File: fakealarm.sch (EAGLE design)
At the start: 14 parts, among them IC1 NE555N, Q1 2N3904, X1 RUN, X2 BAT, X3 GND

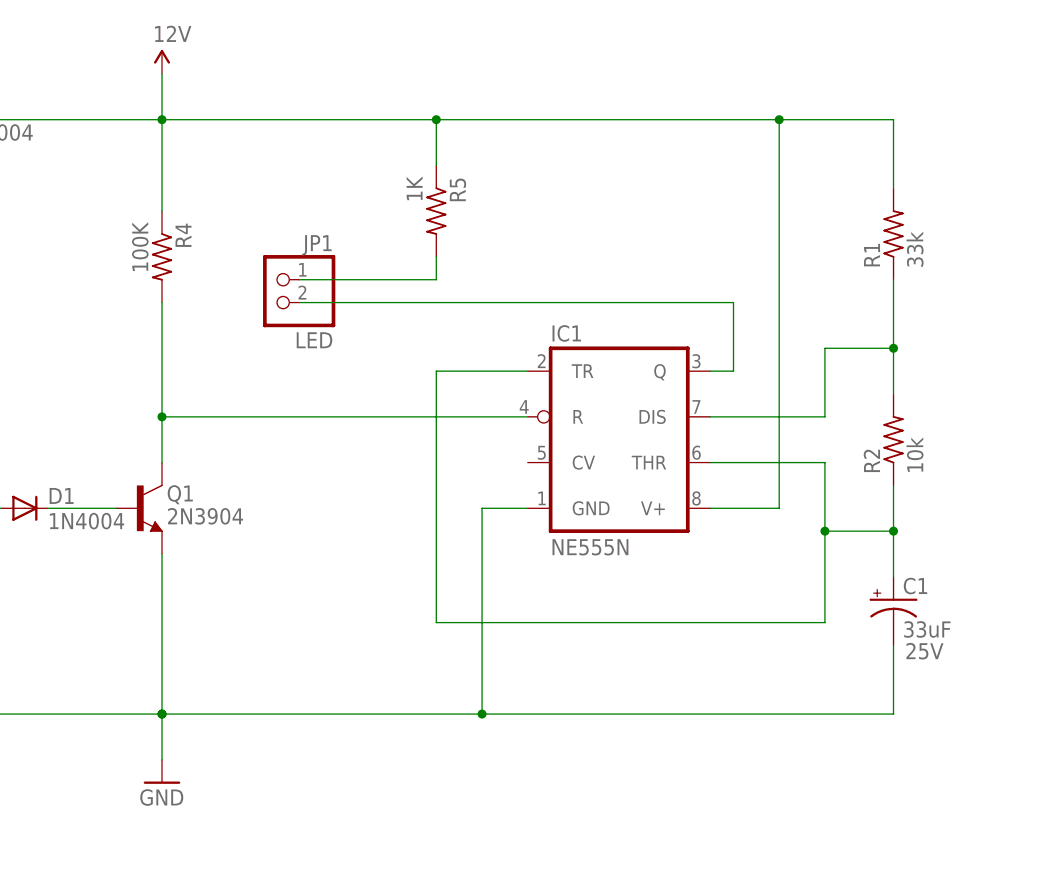
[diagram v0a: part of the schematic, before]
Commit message: Added 10nF (0.01uF) bypass on CV, shrank board, moved components around a little
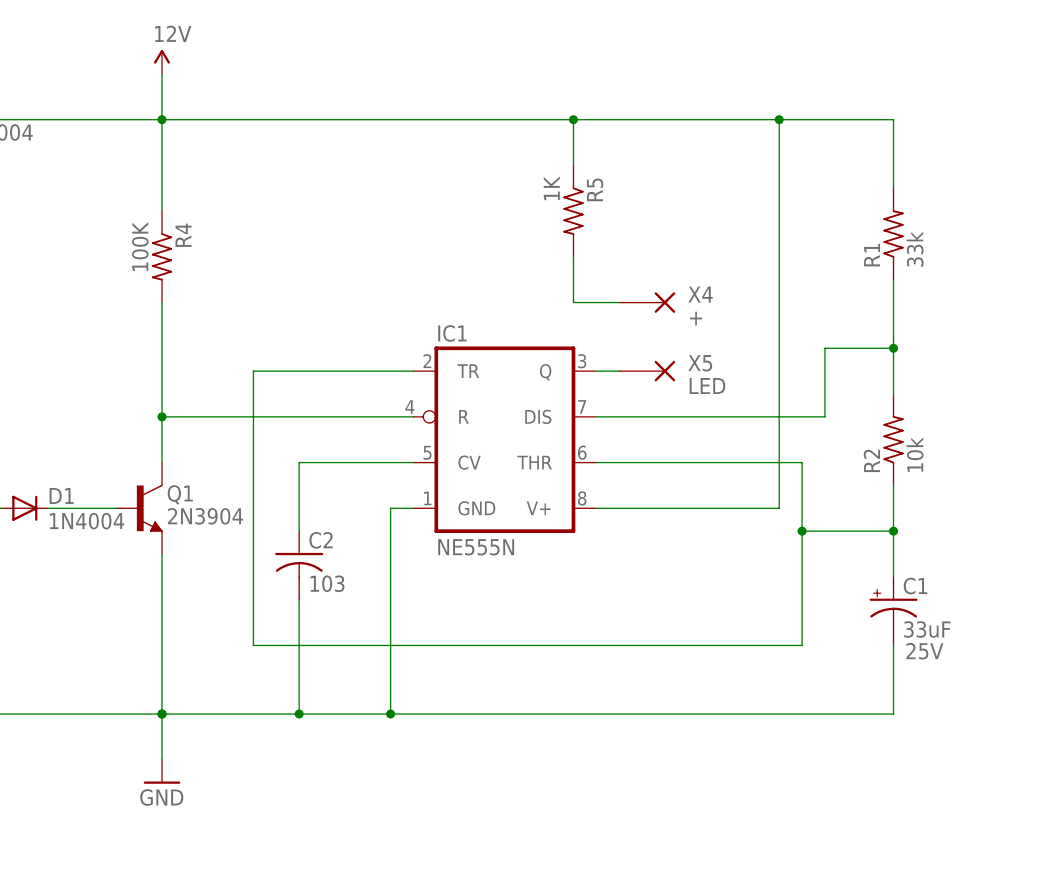
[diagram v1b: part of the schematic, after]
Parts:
- removed JP1: LED, pinhead-2:PINHD-1X02_2.54-S
- added C2: 103, rcl:C-US050-024X044
- added X4: +, bt_electromech:WIREPAD_24GA
- added X5: LED, bt_electromech:WIREPAD_24GA
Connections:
- new net N$7: C2.1, IC1.CV
- net GND: now also C2.2
- net N$10: now also X5.P; no longer JP1.2
- net N$9: now also X4.P; no longer JP1.1
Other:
- moved on the sheet: IC1, R5
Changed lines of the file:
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@@
 <attribute name="VOLTAGE" value="25V"/>
 </part>
-<part name="JP1" library="pinhead-2" deviceset="PINHD-1X02" device="_2.54-S" value="LED"/>
 <part name="SUPPLY1" library="SparkFun-Aesthetics" deviceset="12V" device=""/>
 <part name="GND4" library="bt" deviceset="GND" device=""/>
@@
 <part name="D2" library="diode" deviceset="1N4004" device=""/>
 <part name="FRAME1" library="bt" deviceset="LETTER_L" device=""/>
+<part name="X4" library="bt_electromech" deviceset="WIREPAD" device="_24GA" value="+"/>
+<part name="X5" library="bt_electromech" deviceset="WIREPAD" device="_24GA" value="LED"/>
+<part name="C2" library="rcl" deviceset="C-US" device="050-024X044" value="103"/>
 </parts>
 <sheets>
@@
 </plain>
 <instances>
-<instance part="IC1" gate="A" x="160.02" y="104.14"/>
+<instance part="IC1" gate="A" x="147.32" y="104.14"/>
 <instance part="Q1" gate="G1" x="106.68" y="96.52"/>
 <instance part="R1" gate="G$1" x="190.5" y="127" rot="R90"/>
@@
 <instance part="R3" gate="G$1" x="83.82" y="96.52" rot="R180"/>
 <instance part="R4" gate="G$1" x="109.22" y="124.46" rot="R270"/>
-<instance part="R5" gate="G$1" x="139.7" y="129.54" rot="R270"/>
+<instance part="R5" gate="G$1" x="154.94" y="129.54" rot="R270"/>
 <instance part="C1" gate="G$1" x="190.5" y="86.36">
 <attribute name="VOLTAGE" x="191.77" y="79.756" size="1.778" layer="96"/>
 </instance>
-<instance part="JP1" gate="A" x="121.92" y="119.38" rot="MR0"/>
 <instance part="SUPPLY1" gate="G$1" x="109.22" y="144.78"/>
 <instance part="GND4" gate="1" x="109.22" y="66.04"/>
@@
 <instance part="FRAME1" gate="G$1" x="0" y="0"/>
 <instance part="FRAME1" gate="G$2" x="147.32" y="2.54"/>
+<instance part="X4" gate="G$1" x="165.1" y="119.38"/>
+<instance part="X5" gate="G$1" x="165.1" y="111.76"/>
+<instance part="C2" gate="G$1" x="124.46" y="91.44"/>
 </instances>
 <busses>
@@
 <pinref part="IC1" gate="A" pin="DIS"/>
 <wire x1="190.5" y1="114.3" x2="190.5" y2="109.22" width="0.1524" layer="91"/>
-<wire x1="170.18" y1="106.68" x2="182.88" y2="106.68" width="0.1524" layer="91"/>
+<wire x1="157.48" y1="106.68" x2="182.88" y2="106.68" width="0.1524" layer="91"/>
 <wire x1="182.88" y1="106.68" x2="182.88" y2="114.3" width="0.1524" layer="91"/>
 <wire x1="182.88" y1="114.3" x2="190.5" y2="114.3" width="0.1524" layer="91"/>
@@
 <pinref part="IC1" gate="A" pin="TR"/>
 <wire x1="190.5" y1="93.98" x2="190.5" y2="99.06" width="0.1524" layer="91"/>
-<wire x1="149.86" y1="111.76" x2="139.7" y2="111.76" width="0.1524" layer="91"/>
-<wire x1="139.7" y1="111.76" x2="139.7" y2="83.82" width="0.1524" layer="91"/>
-<wire x1="139.7" y1="83.82" x2="182.88" y2="83.82" width="0.1524" layer="91"/>
-<wire x1="182.88" y1="83.82" x2="182.88" y2="93.98" width="0.1524" layer="91"/>
-<wire x1="182.88" y1="93.98" x2="190.5" y2="93.98" width="0.1524" layer="91"/>
+<wire x1="137.16" y1="111.76" x2="119.38" y2="111.76" width="0.1524" layer="91"/>
+<wire x1="119.38" y1="111.76" x2="119.38" y2="81.28" width="0.1524" layer="91"/>
+<wire x1="119.38" y1="81.28" x2="180.34" y2="81.28" width="0.1524" layer="91"/>
+<wire x1="180.34" y1="81.28" x2="180.34" y2="93.98" width="0.1524" layer="91"/>
+<wire x1="180.34" y1="93.98" x2="190.5" y2="93.98" width="0.1524" layer="91"/>
 <junction x="190.5" y="93.98"/>
 <pinref part="IC1" gate="A" pin="THR"/>
-<wire x1="170.18" y1="101.6" x2="182.88" y2="101.6" width="0.1524" layer="91"/>
-<wire x1="182.88" y1="101.6" x2="182.88" y2="93.98" width="0.1524" layer="91"/>
-<junction x="182.88" y="93.98"/>
+<wire x1="157.48" y1="101.6" x2="180.34" y2="101.6" width="0.1524" layer="91"/>
+<wire x1="180.34" y1="101.6" x2="180.34" y2="93.98" width="0.1524" layer="91"/>
+<junction x="180.34" y="93.98"/>
 </segment>
 </net>
@@
 <junction x="109.22" y="73.66"/>
 <junction x="109.22" y="73.66"/>
-<wire x1="109.22" y1="73.66" x2="144.78" y2="73.66" width="0.1524" layer="91"/>
 <pinref part="C1" gate="G$1" pin="-"/>
-<wire x1="144.78" y1="73.66" x2="190.5" y2="73.66" width="0.1524" layer="91"/>
+<pinref part="C2" gate="G$1" pin="2"/>
+<wire x1="124.46" y1="86.36" x2="124.46" y2="73.66" width="0.1524" layer="91"/>
+<wire x1="124.46" y1="73.66" x2="134.62" y2="73.66" width="0.1524" layer="91"/>
+<wire x1="134.62" y1="73.66" x2="190.5" y2="73.66" width="0.1524" layer="91"/>
 <wire x1="190.5" y1="73.66" x2="190.5" y2="81.28" width="0.1524" layer="91"/>
+<wire x1="109.22" y1="73.66" x2="124.46" y2="73.66" width="0.1524" layer="91"/>
+<junction x="124.46" y="73.66"/>
 <pinref part="IC1" gate="A" pin="GND"/>
-<wire x1="149.86" y1="96.52" x2="144.78" y2="96.52" width="0.1524" layer="91"/>
-<wire x1="144.78" y1="96.52" x2="144.78" y2="73.66" width="0.1524" layer="91"/>
-<junction x="144.78" y="73.66"/>
+<wire x1="137.16" y1="96.52" x2="134.62" y2="96.52" width="0.1524" layer="91"/>
+<wire x1="134.62" y1="96.52" x2="134.62" y2="73.66" width="0.1524" layer="91"/>
+<junction x="134.62" y="73.66"/>
 </segment>
 </net>
 <net name="N$9" class="0">
 <segment>
-<pinref part="JP1" gate="A" pin="1"/>
 <pinref part="R5" gate="G$1" pin="2"/>
-<wire x1="139.7" y1="124.46" x2="139.7" y2="121.92" width="0.1524" layer="91"/>
-<wire x1="139.7" y1="121.92" x2="124.46" y2="121.92" width="0.1524" layer="91"/>
+<wire x1="154.94" y1="124.46" x2="154.94" y2="119.38" width="0.1524" layer="91"/>
+<wire x1="154.94" y1="119.38" x2="160.02" y2="119.38" width="0.1524" layer="91"/>
+<pinref part="X4" gate="G$1" pin="P"/>
 </segment>
 </net>
@@
 <pinref part="R1" gate="G$1" pin="2"/>
 <wire x1="86.36" y1="139.7" x2="109.22" y2="139.7" width="0.1524" layer="91"/>
-<wire x1="109.22" y1="139.7" x2="139.7" y2="139.7" width="0.1524" layer="91"/>
-<wire x1="139.7" y1="139.7" x2="177.8" y2="139.7" width="0.1524" layer="91"/>
+<wire x1="109.22" y1="139.7" x2="154.94" y2="139.7" width="0.1524" layer="91"/>
+<wire x1="154.94" y1="139.7" x2="177.8" y2="139.7" width="0.1524" layer="91"/>
 <wire x1="177.8" y1="139.7" x2="190.5" y2="139.7" width="0.1524" layer="91"/>
 <wire x1="190.5" y1="139.7" x2="190.5" y2="132.08" width="0.1524" layer="91"/>
@@
 <wire x1="109.22" y1="139.7" x2="109.22" y2="144.78" width="0.1524" layer="91"/>
 <pinref part="R5" gate="G$1" pin="1"/>
-<wire x1="139.7" y1="134.62" x2="139.7" y2="139.7" width="0.1524" layer="91"/>
-<junction x="139.7" y="139.7"/>
+<wire x1="154.94" y1="134.62" x2="154.94" y2="139.7" width="0.1524" layer="91"/>
+<junction x="154.94" y="139.7"/>
 <pinref part="IC1" gate="A" pin="V+"/>
-<wire x1="170.18" y1="96.52" x2="177.8" y2="96.52" width="0.1524" layer="91"/>
+<wire x1="157.48" y1="96.52" x2="177.8" y2="96.52" width="0.1524" layer="91"/>
 <wire x1="177.8" y1="96.52" x2="177.8" y2="139.7" width="0.1524" layer="91"/>
 <junction x="177.8" y="139.7"/>
@@
 <segment>
 <pinref part="IC1" gate="A" pin="Q"/>
-<wire x1="170.18" y1="111.76" x2="172.72" y2="111.76" width="0.1524" layer="91"/>
-<wire x1="172.72" y1="111.76" x2="172.72" y2="119.38" width="0.1524" layer="91"/>
-<pinref part="JP1" gate="A" pin="2"/>
-<wire x1="172.72" y1="119.38" x2="124.46" y2="119.38" width="0.1524" layer="91"/>
+<wire x1="157.48" y1="111.76" x2="160.02" y2="111.76" width="0.1524" layer="91"/>
+<pinref part="X5" gate="G$1" pin="P"/>
 </segment>
 </net>
@@
 <segment>
 <pinref part="IC1" gate="A" pin="R"/>
-<wire x1="149.86" y1="106.68" x2="109.22" y2="106.68" width="0.1524" layer="91"/>
+<wire x1="137.16" y1="106.68" x2="109.22" y2="106.68" width="0.1524" layer="91"/>
 <pinref part="Q1" gate="G1" pin="C"/>
 <pinref part="R4" gate="G$1" pin="2"/>
@@
 </segment>
 </net>
+<net name="N$7" class="0">
+<segment>
+<pinref part="IC1" gate="A" pin="CV"/>
+<pinref part="C2" gate="G$1" pin="1"/>
+<wire x1="137.16" y1="101.6" x2="124.46" y2="101.6" width="0.1524" layer="91"/>
+<wire x1="124.46" y1="101.6" x2="124.46" y2="93.98" width="0.1524" layer="91"/>
+</segment>
+</net>

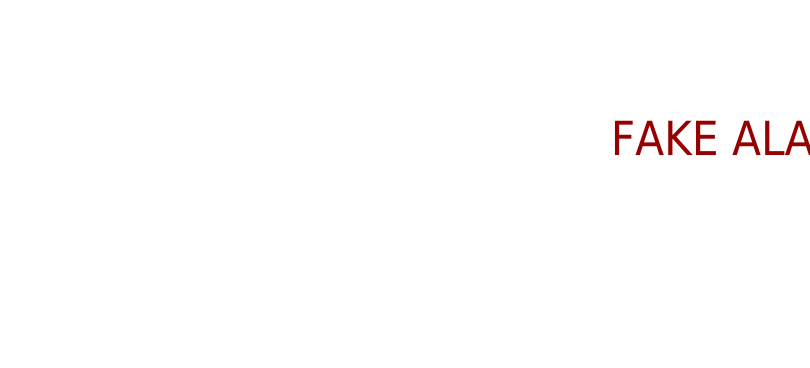
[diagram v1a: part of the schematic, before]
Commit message: added oshw logo, minor silk layout tweaks
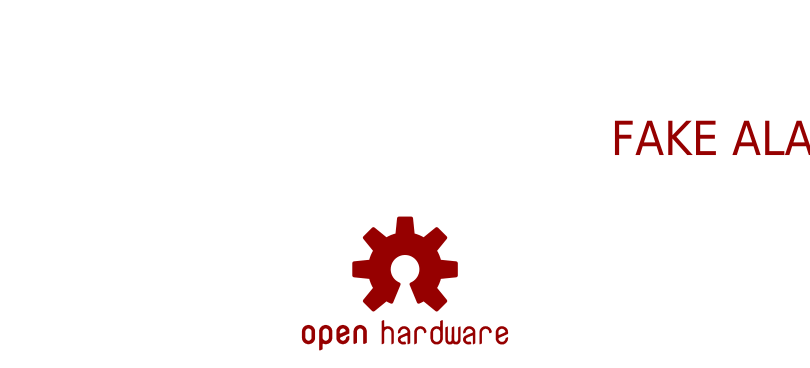
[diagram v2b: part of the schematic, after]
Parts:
- added LOGO1: OSHW-LOGOS, SparkFun-Aesthetics:OSHW-LOGOS
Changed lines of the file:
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@@
 <part name="X5" library="bt_electromech" deviceset="WIREPAD" device="_24GA" value="LED"/>
 <part name="C2" library="rcl" deviceset="C-US" device="050-024X044" value="103"/>
+<part name="LOGO1" library="SparkFun-Aesthetics" deviceset="OSHW-LOGO" device="S" value="OSHW-LOGOS"/>
 </parts>
 <sheets>
@@
 <instance part="X5" gate="G$1" x="165.1" y="111.76"/>
 <instance part="C2" gate="G$1" x="124.46" y="91.44"/>
+<instance part="LOGO1" gate="G$1" x="132.08" y="10.16"/>
 </instances>
 <busses>

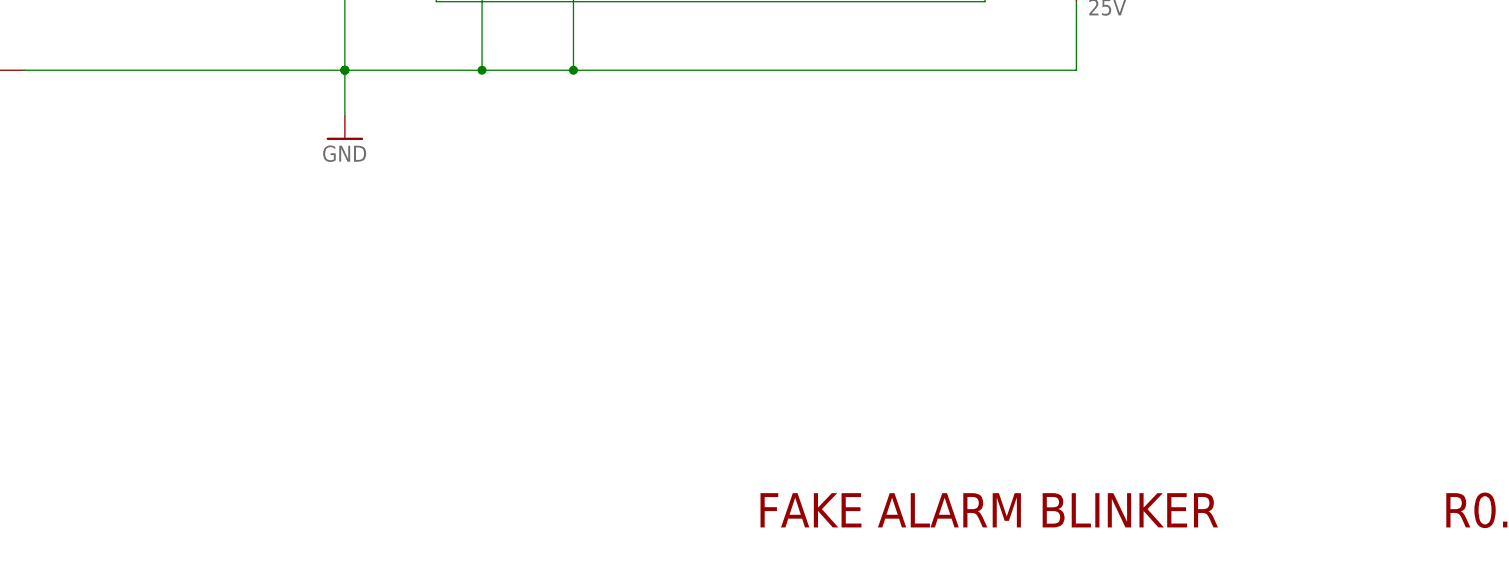
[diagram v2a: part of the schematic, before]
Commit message: Generated silk, added enclosure info to schematic
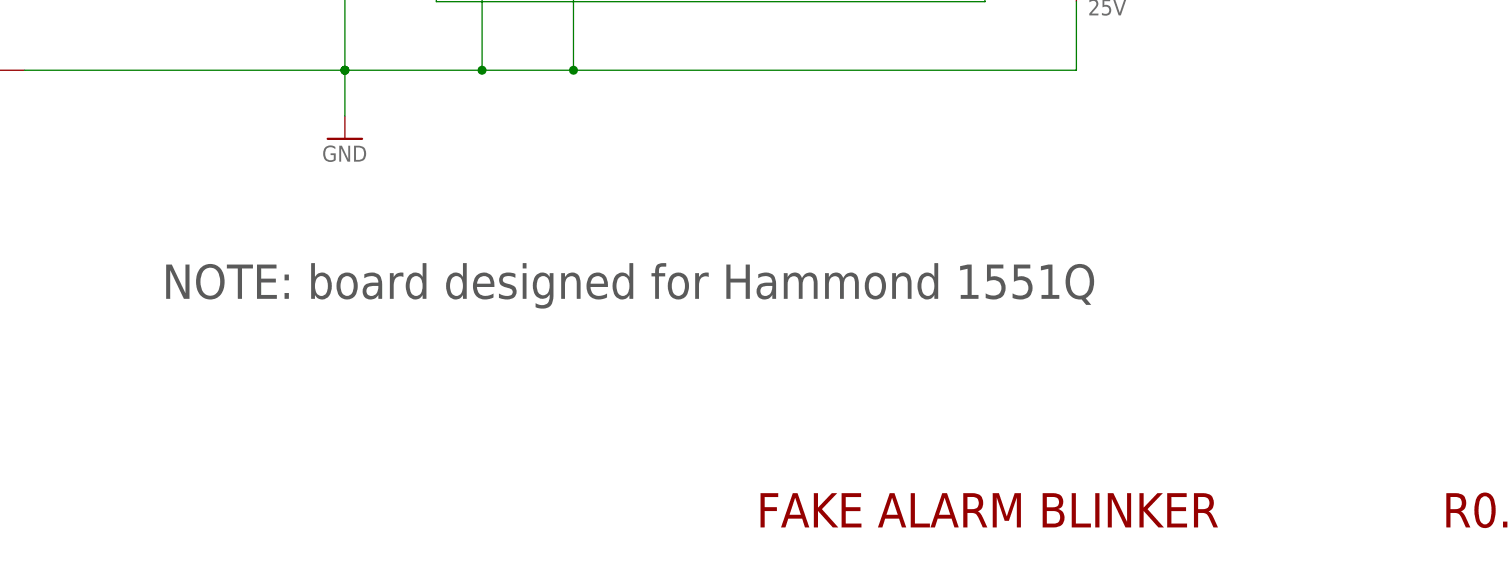
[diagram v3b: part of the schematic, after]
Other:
- note added: "NOTE: board designed for Hammond 1551Q"
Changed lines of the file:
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@@
 <text x="154.94" y="22.86" size="3.81" layer="94">FAKE ALARM BLINKER</text>
 <text x="231.14" y="22.86" size="3.81" layer="94">R0.1</text>
+<text x="88.9" y="48.26" size="3.81" layer="97">NOTE: board designed for Hammond 1551Q</text>
 </plain>
 <instances>
